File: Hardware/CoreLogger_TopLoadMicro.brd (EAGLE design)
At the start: 80 x 80 mm, 75 parts, among them J1 CONN_32.54_SCREW, J10 CONN_42.54_SCREW, J11 CONN_32.54_SCREW, J12 CONN_32.54_SCREW, J13 CONN_62.54, J2 CONN_32.54_SCREW, J4 CONN_5, J6 CONN_42.54_SCREW, J7 CONN_42.54_SCREW, J8 CONN_42.54_SCREW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

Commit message: Generated optional board designs, generated gerbers
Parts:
- removed R41: 10k, bschulz_passives:R0402
- SD1: value MICROSDCD -> MICROSD_NOCDHINDGED; device bschulz:MICROSD_CD -> bschulz:USD_MOLEX_HINDGED
- moved SD1 7.27 mm to (2.42, 43.5), turned to 270 degrees
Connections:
- net 3V3: no longer R41.2
- net GND: now also SD1.BODY@1, SD1.BODY@2, SD1.BODY@3, SD1.BODY@4; no longer SD1.CD2, SD1.MT1, SD1.MT2, SD1.MT3, SD1.MT4
- net SD_CD: no longer R41.1, SD1.CD1
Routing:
- net SD_CD: track 19.7 -> 0.00 mm
- net GND: track 602.6 -> 590.1 mm
- net 3V3: track 283.1 -> 274.6 mm
- net MISO: track 69.8 -> 68.0 mm
- net SCK: track 56.1 -> 54.4 mm
- net MOSI: track 61.8 -> 60.2 mm
- net SD_CS: track 63.6 -> 62.0 mm

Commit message: Added BoM info and software for Lidar Lite interface
Updated the BoM information in Eagle and generated csv, also added software for LidarLite interface system
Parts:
- R10, R11: value 10M -> 180k

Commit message: Minor cleanup
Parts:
- R5: value (none) -> 1k
- R6: value (none) -> 470
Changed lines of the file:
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@@
 <attribute name="VALUE_PART" value="180k" x="-8.509" y="150.368" size="1.778" layer="27" rot="R180" display="off"/>
 </element>
-<element name="R5" library="bschulz_passives" package="R0603" value="" x="69.342" y="43.688" smashed="yes" rot="R90">
+<element name="R5" library="bschulz_passives" package="R0603" value="1k" x="69.342" y="43.688" smashed="yes" rot="R90">
 <attribute name="DIGIKEY" value="311-1KLDCT-ND" x="154.432" y="93.218" size="1.778" layer="27" rot="R90" display="off"/>
 <attribute name="MF" value="Yageo" x="154.432" y="93.218" size="1.778" layer="27" rot="R90" display="off"/>
@@
 <attribute name="VALUE_PART" value="1k" x="154.432" y="93.218" size="1.778" layer="27" rot="R90" display="off"/>
 </element>
-<element name="R6" library="bschulz_passives" package="R0603" value="" x="78.105" y="43.688" smashed="yes" rot="R90">
+<element name="R6" library="bschulz_passives" package="R0603" value="470" x="78.105" y="43.688" smashed="yes" rot="R90">
 <attribute name="DIGIKEY" value="311-470HRCT-ND" x="163.195" y="97.028" size="1.778" layer="27" rot="R90" display="off"/>
 <attribute name="MF" value="Yageo" x="163.195" y="97.028" size="1.778" layer="27" rot="R90" display="off"/>

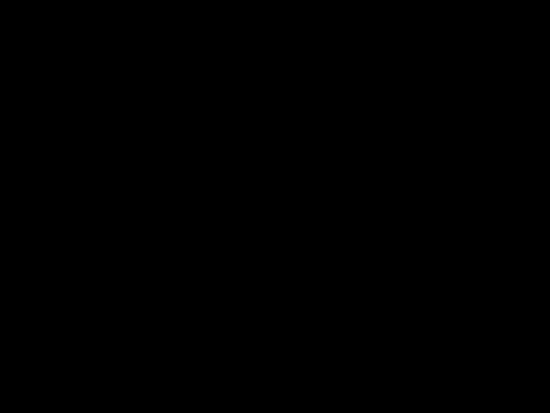
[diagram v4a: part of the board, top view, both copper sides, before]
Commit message: Added Sap Heater FET pullup
Added gate pullup to the FET drive on the sap heater power system
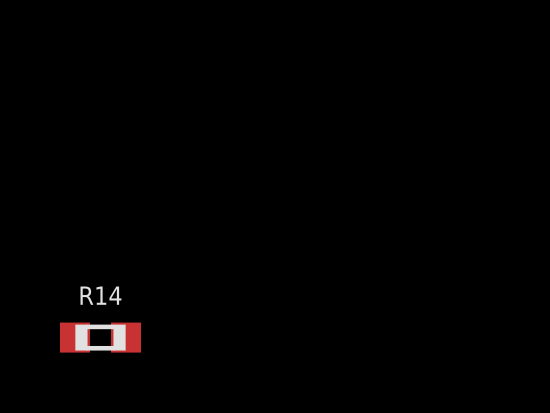
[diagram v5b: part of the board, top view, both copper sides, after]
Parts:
- added R14: 180k, bschulz_passives:R0603
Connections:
- net 3V3: now also R14.2
- net SAP_HEATER_SW: now also R14.1
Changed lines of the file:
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@@
 <attribute name="VALUE" x="27.051" y="16.637" size="1.27" layer="27" rot="R180"/>
+</element>
+<element name="R14" library="bschulz_passives" package="R0603" value="180k" x="-3.81" y="-7.62" smashed="yes">
+<attribute name="DIGIKEY" value="P180KHCT-ND" x="-3.81" y="-7.62" size="1.778" layer="27" display="off"/>
+<attribute name="MF" value="Panasonic" x="-3.81" y="-7.62" size="1.778" layer="27" display="off"/>
+<attribute name="MPN" value="ERJ-3EKF1803V" x="-3.81" y="-7.62" size="1.778" layer="27" display="off"/>
+<attribute name="NAME" x="-3.81" y="-6.223" size="0.6096" layer="25" font="vector" ratio="15" align="center"/>
+<attribute name="VALUE" x="-3.81" y="-9.017" size="0.6096" layer="27" font="vector" ratio="15" align="center"/>
+<attribute name="VALUE_PART" value="180k" x="-3.81" y="-7.62" size="1.778" layer="27" display="off"/>
 </element>
 </elements>
@@
 <wire x1="7.14935" y1="34.4996" x2="7.1564" y2="34.4996" width="0.2" layer="1"/>
 <wire x1="4.3486" y1="34.6404" x2="7.00855" y2="34.6404" width="0.2" layer="1"/>
+<contactref element="R14" pad="2"/>
+<wire x1="-2.96" y1="-7.62" x2="19.431" y2="13.462" width="0" layer="19" extent="1-1"/>
 </signal>
 <signal name="SCL">
@@
 <wire x1="13.081" y1="67.183" x2="21.844" y2="58.42" width="0.254" layer="16"/>
 <wire x1="21.844" y1="58.42" x2="21.844" y2="57.531" width="0.254" layer="16"/>
+<contactref element="R14" pad="1"/>
+<wire x1="-4.66" y1="-7.62" x2="35.814" y2="24.257" width="0" layer="19" extent="1-1"/>
 </signal>
 <signal name="AUX_EN">
